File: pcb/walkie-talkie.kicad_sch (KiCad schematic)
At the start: 11 parts

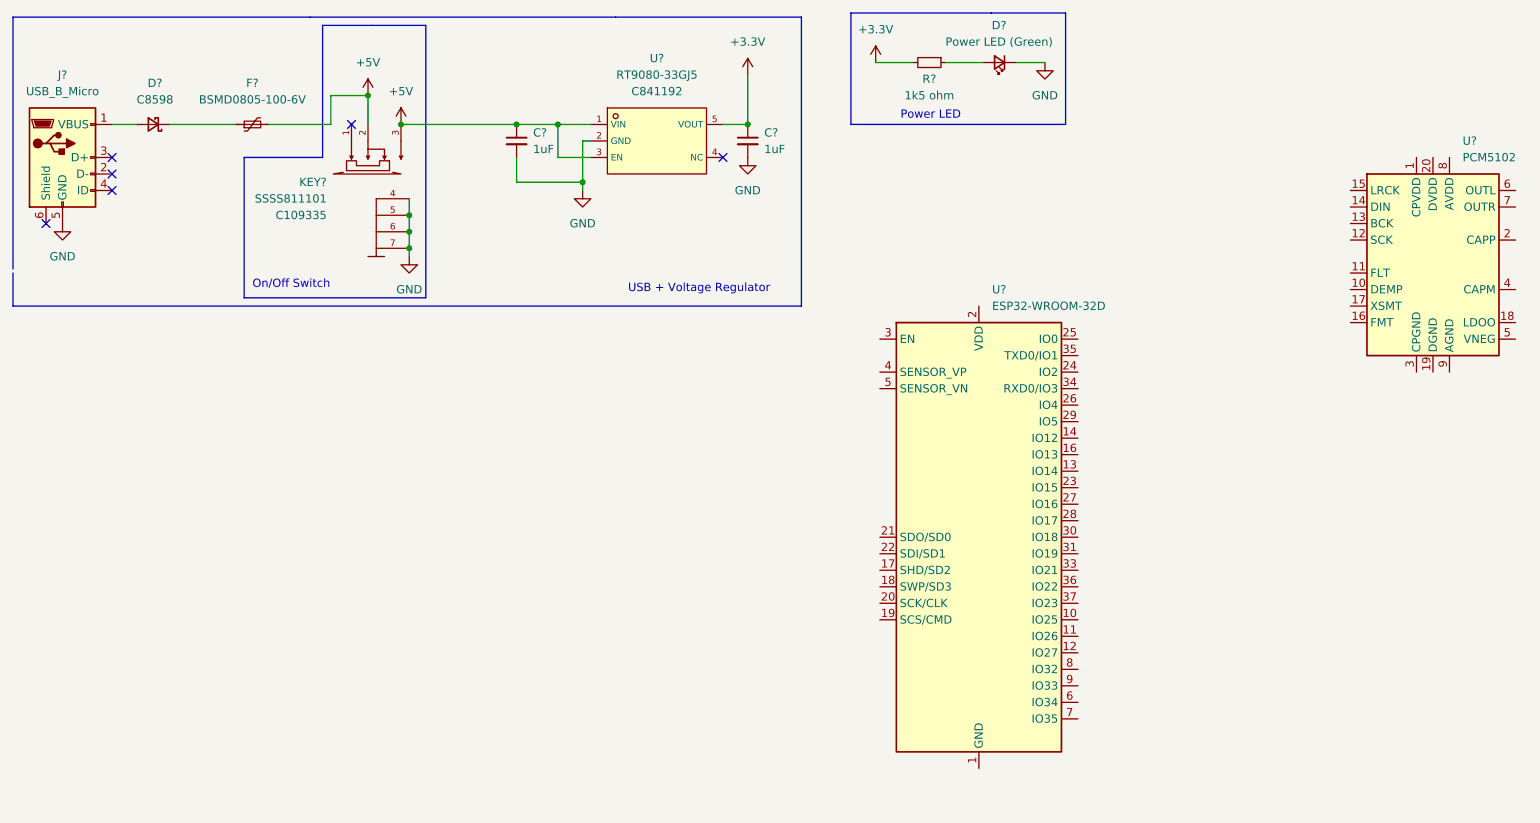
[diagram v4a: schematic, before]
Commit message: Add a headphone jack
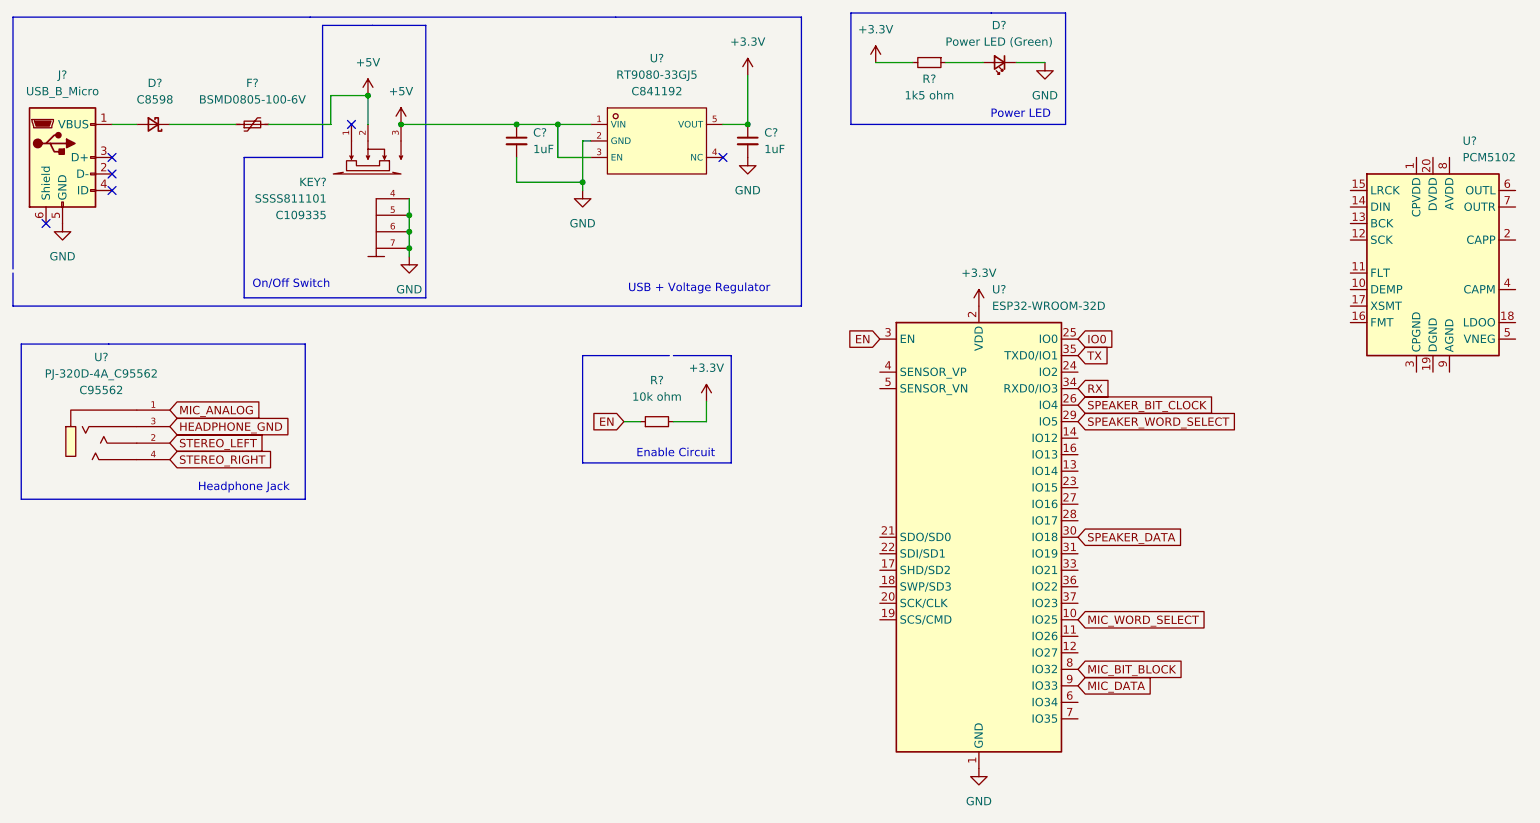
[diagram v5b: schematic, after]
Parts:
- added R?: 10k ohm, symbol Device:R_Small
- added U?: PJ-320D-4A_C95562, footprint:AUDIO-SMD_PJ-320D-4A, symbol pj-320d-4a:PJ-320D-4A_C95562
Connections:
- net +3V3: now also U?.2 (VDD), R?.2
- net GND: now also U?.1 (GND), U?.15 (GND), U?.38 (GND), U?.39 (GND)
- net MIC_WORD_SELECT: now reaches U?.10 (IO25)
- net IO0: now reaches U?.25 (IO0)
- net SPEAKER_BIT_CLOCK: now reaches U?.26 (IO4)
- net SPEAKER_WORD_SELECT: now reaches U?.29 (IO5)
- net EN: now reaches U?.3 (EN)
- net EN: now also R?.1
- net SPEAKER_DATA: now reaches U?.30 (IO18)
- net RX: now reaches U?.34 (RXD0/IO3)
- net TX: now reaches U?.35 (TXD0/IO1)
- net MIC_BIT_BLOCK: now reaches U?.8 (IO32)
- net MIC_DATA: now reaches U?.9 (IO33)
- new net HEADPHONE_GND: U?.3
- new net MIC_ANALOG: U?.1
- new net STEREO_LEFT: U?.2
- new net STEREO_RIGHT: U?.4
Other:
- note added: "Enable Circuit"
- note added: "Headphone Jack"

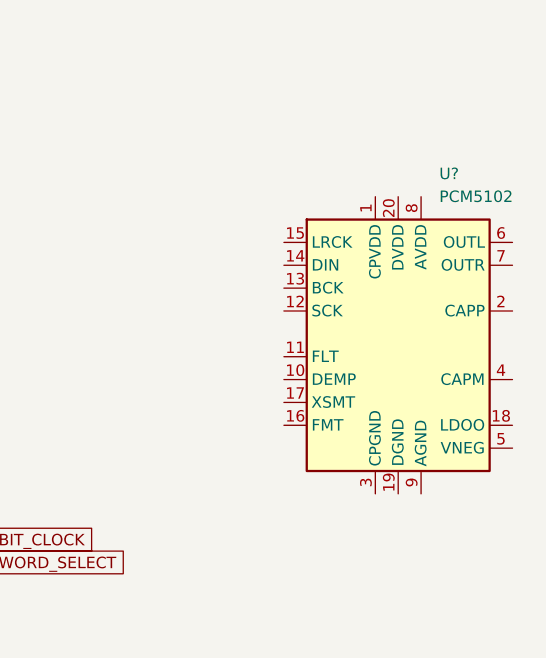
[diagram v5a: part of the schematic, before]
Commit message: Remove PCM5102 for now
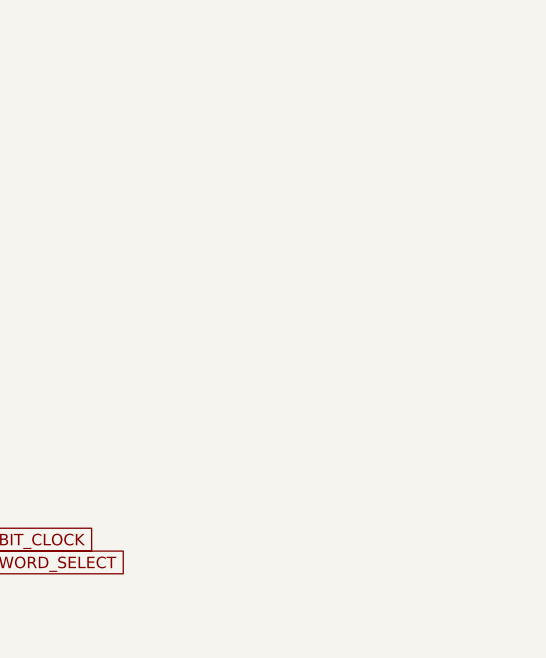
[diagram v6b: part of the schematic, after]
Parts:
- removed U?: PCM5102, Package_SO:TSSOP-20_4.4x6.5mm_P0.65mm, symbol Audio:PCM5102
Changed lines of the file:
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@@
     (pin "5")
-  )
-  (symbol (lib_id "Audio:PCM5102") (at 233.68 50.8 0) (unit 1)
-    (in_bom yes) (on_board yes) (fields_autoplaced)
-    (property "Reference" "U?" (id 0) (at 238.2394 33.02 0)
-      (effects (font (size 1.27 1.27)) (justify left))
-    )
-    (property "Value" "PCM5102" (id 1) (at 238.2394 35.56 0)
-      (effects (font (size 1.27 1.27)) (justify left))
-    )
-    (property "Footprint" "Package_SO:TSSOP-20_4.4x6.5mm_P0.65mm" (id 2) (at 232.41 31.75 0)
-      (effects (font (size 1.27 1.27)) hide)
-    )
-    (property "Datasheet" "http://www.ti.com/lit/ds/symlink/pcm5102.pdf" (id 3) (at 232.41 31.75 0)
-      (effects (font (size 1.27 1.27)) hide)
-    )
-    (pin "1")
-    (pin "10")
-    (pin "11")
-    (pin "12")
-    (pin "13")
-    (pin "14")
-    (pin "15")
-    (pin "16")
-    (pin "17")
-    (pin "18")
-    (pin "19")
-    (pin "2")
-    (pin "20")
-    (pin "3")
-    (pin "4")
-    (pin "5")
-    (pin "6")
-    (pin "7")
-    (pin "8")
-    (pin "9")
   )
   (symbol (lib_id "power:+3.3V") (at 128.27 22.86 0) (unit 1)
@@
       (reference "U?") (unit 1) (value "RT9080-33GJ5") (footprint "footprint:TSOT-23-5_L2.9-W1.6-P0.95-LS2.8-BL")
     )
-    (path "/cf89533d-ed9d-47a8-9bf7-db1237da3977"
-      (reference "U?") (unit 1) (value "PCM5102") (footprint "Package_SO:TSSOP-20_4.4x6.5mm_P0.65mm")
-    )
     (path "/fc4e87c7-84e4-4123-82fc-bb2383e03194"
